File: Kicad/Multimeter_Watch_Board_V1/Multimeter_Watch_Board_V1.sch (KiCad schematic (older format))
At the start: 30 parts, among them J1 AudioJack3_Ground_renamedPins, J2 AudioJack3_Ground_renamedPins, J3 AudioJack3_Ground_renamedPins, J4 Conn_01x16_Female, J5 Conn_01x16_Female, U1 PCF85163-SO08, U2 AD8592, Y1 32kHz

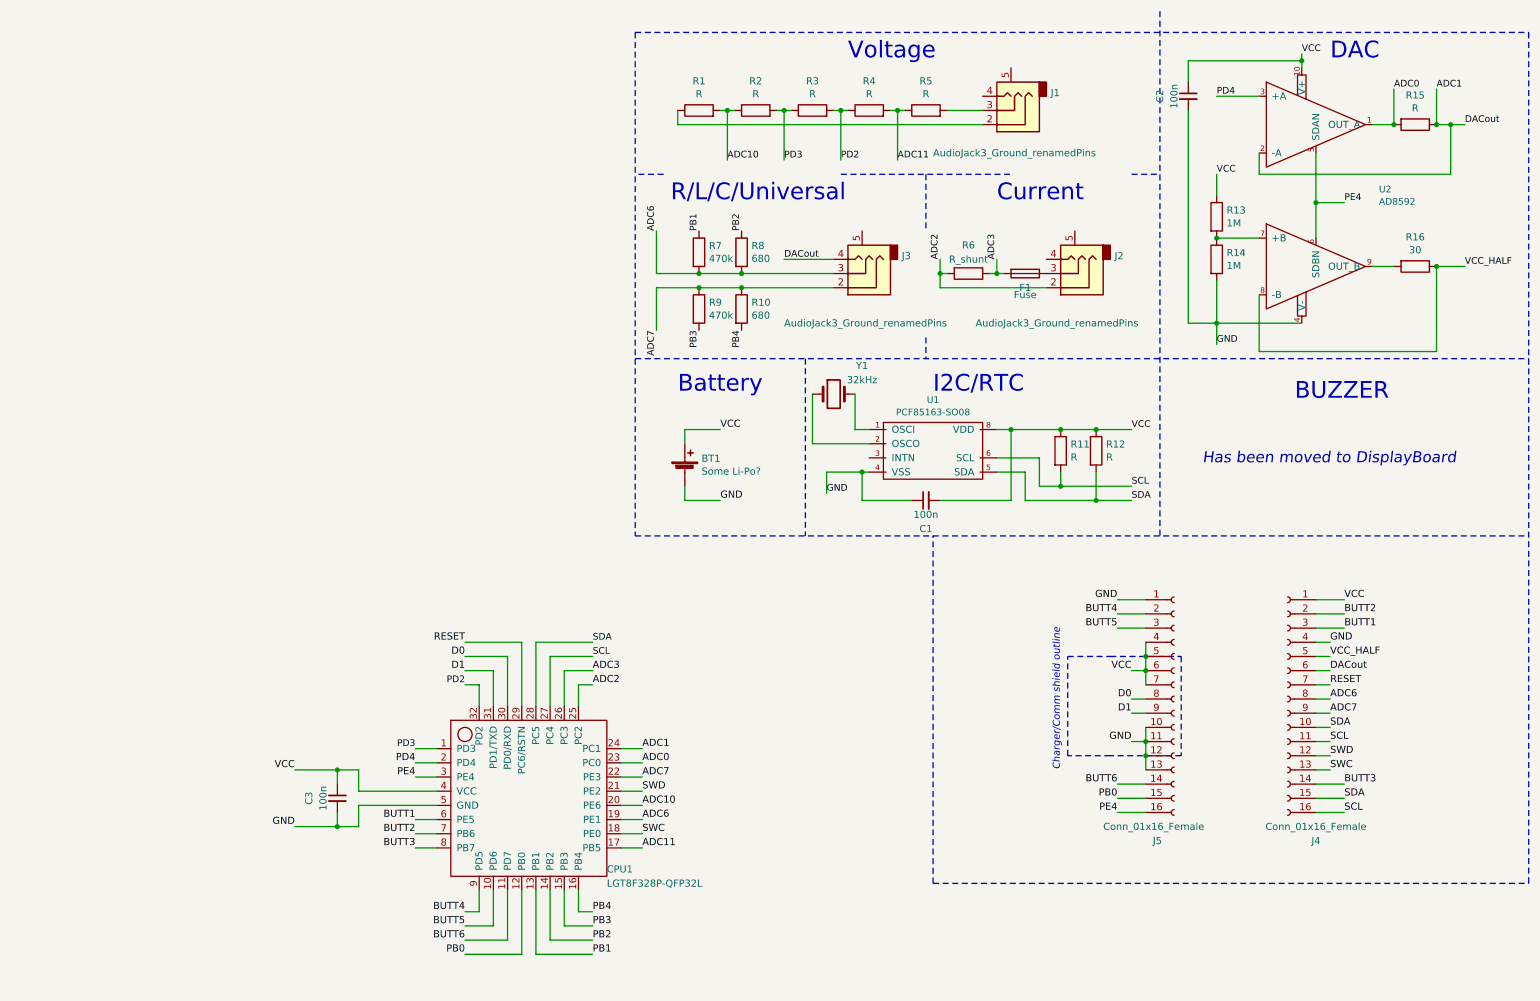
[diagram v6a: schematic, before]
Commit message: second layout attempt, various pinout changes for better routing
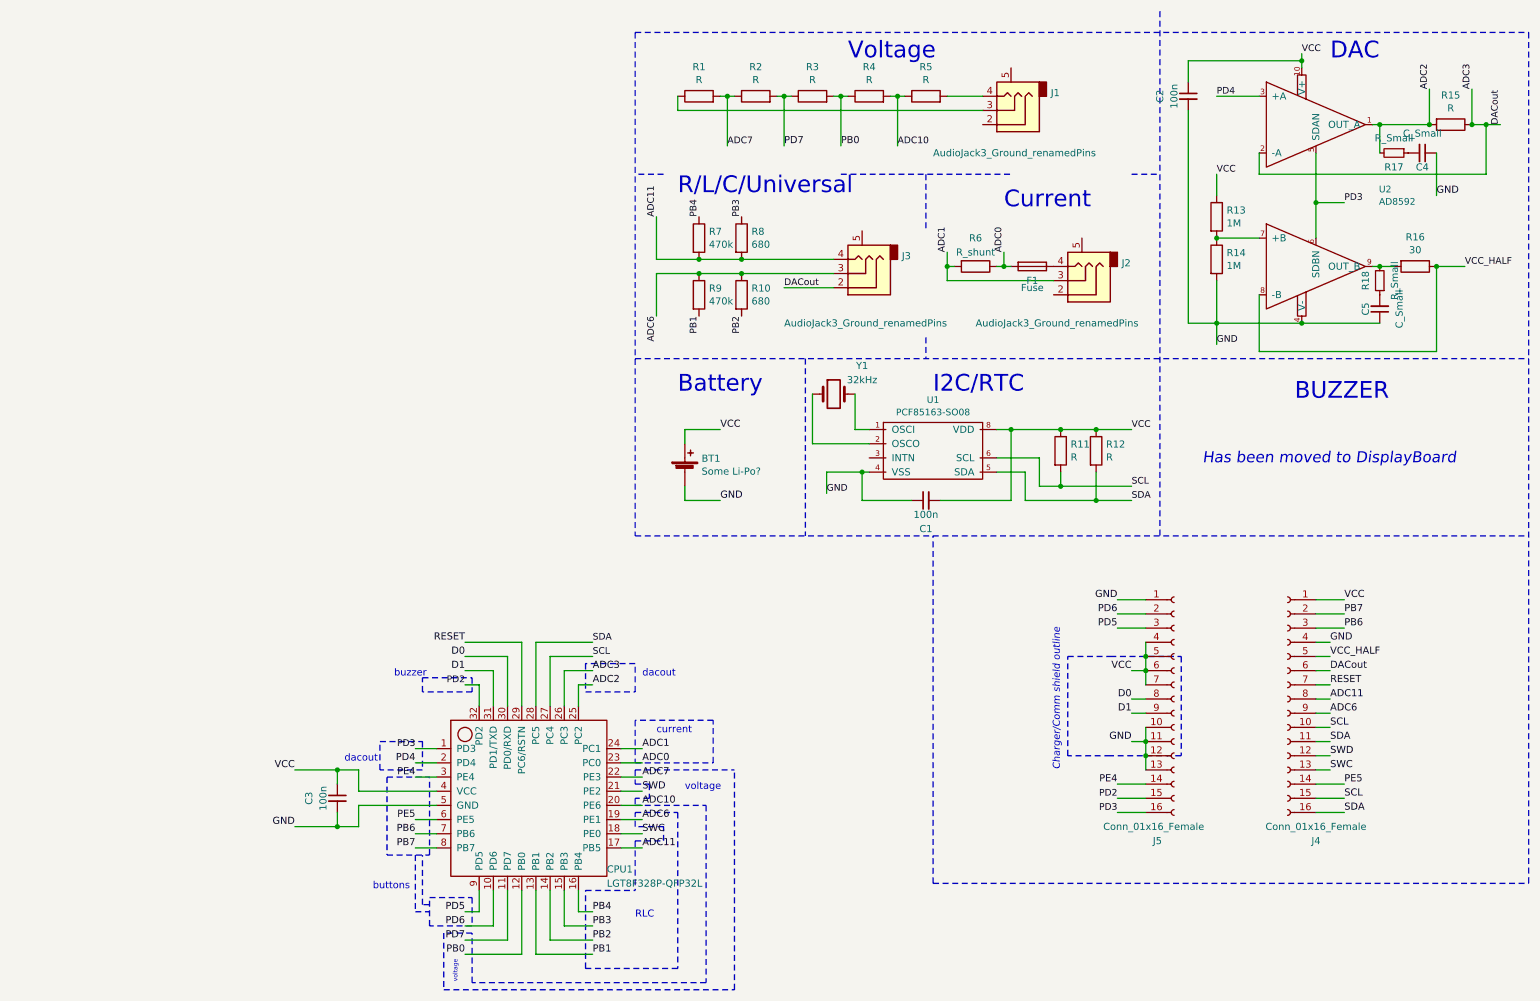
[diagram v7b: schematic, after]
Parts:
- added C4, C5: C_Small, Capacitor_SMD:C_0805_2012Metric_Pad1.15x1.40mm_HandSolder, symbol Device:C_Small
- added R17, R18: R_Small, Resistor_SMD:R_0805_2012Metric_Pad1.15x1.40mm_HandSolder, symbol Device:R_Small
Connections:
- net ADC0: now also F1.2, R6.1; no longer R15.2, U2.1 (OUT_A)
- net ADC1: now also J2.3, R6.2; no longer J3.4, J4.6 (Pin_6), R15.1, U2.2 (-A)
- net ADC10: now also R4.2, R5.1; no longer R1.2, R2.1
- net ADC11: now also J3.4, J4.8 (Pin_8), R7.2, R8.2; no longer R4.2, R5.1
- net ADC2: now also R15.2, U2.1 (OUT_A), R17.2; no longer J2.2, R6.2
- net ADC3: now also J3.2, J4.6 (Pin_6), R15.1, U2.2 (-A); no longer F1.2, R6.1
- net ADC6: now also J4.9 (Pin_9), R10.1, R9.1; no longer J4.8 (Pin_8), R7.2, R8.2
- net ADC7: now also R1.2, R2.1; no longer J3.2, J4.9 (Pin_9), R10.1, R9.1
- net GND: now also C4.1, C5.1
- net PB0: now also R3.2, R4.1; no longer J5.15 (Pin_15)
- net PB1: now also R9.2; no longer R7.1
- net PB2: now also R10.2; no longer R8.1
- net PB3: now also R8.1; no longer R9.2
- net PB4: now also R7.1; no longer R10.2
- net PD2: now also J5.15 (Pin_15); no longer R3.2, R4.1
- net PD3: now also J5.16 (Pin_16), U2.5 (SDAN), U2.6 (SDBN); no longer R2.2, R3.1
- net PE4: now also J5.14 (Pin_14); no longer J5.16 (Pin_16), U2.5 (SDAN), U2.6 (SDBN)
- net SCL: now also J4.10 (Pin_10), J4.15 (Pin_15); no longer J4.11 (Pin_11), J4.16 (Pin_16)
- net SDA: now also J4.11 (Pin_11), J4.16 (Pin_16); no longer J4.10 (Pin_10), J4.15 (Pin_15)
- net at R5.2: now also J1.4; no longer J1.3
- net at R1.1: now also J1.3; no longer J1.2
- net at F1.1: now also J2.4; no longer J2.3
- net at R16.2, U2.9 (OUT_B): now also R18.2
- net BUTT1 renamed PB6
- net PB6: now also CPU1.7 (PB6); no longer CPU1.6 (PE5)
- net BUTT2 renamed PB7
- net PB7: now also CPU1.8 (PB7); no longer CPU1.7 (PB6)
- net BUTT3 renamed PE5
- net PE5: now also CPU1.6 (PE5); no longer CPU1.8 (PB7)
- net BUTT4 renamed PD5
- net PD5: now also J5.3 (Pin_3); no longer J5.2 (Pin_2)
- net BUTT5 renamed PD6
- net PD6: now also J5.2 (Pin_2); no longer J5.3 (Pin_3)
- net BUTT6 renamed PD7
- net PD7: now also R2.2, R3.1; no longer J5.14 (Pin_14)
- new net: C4.2, R17.1
- new net: C5.2, R18.1
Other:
- note added: "RLC\n"
- note added: "buttons\n"
- note added: "buzzer"
- note added: "current\n"
- note added: "dacout"
- note added: "dacout\n"
- note added: "voltage\n"
- moved on the sheet: F1, J2, R1, R10, R15, R2, R3, R4, R5, R6, R7, R8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

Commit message: move I2C pullups from VCC to enable
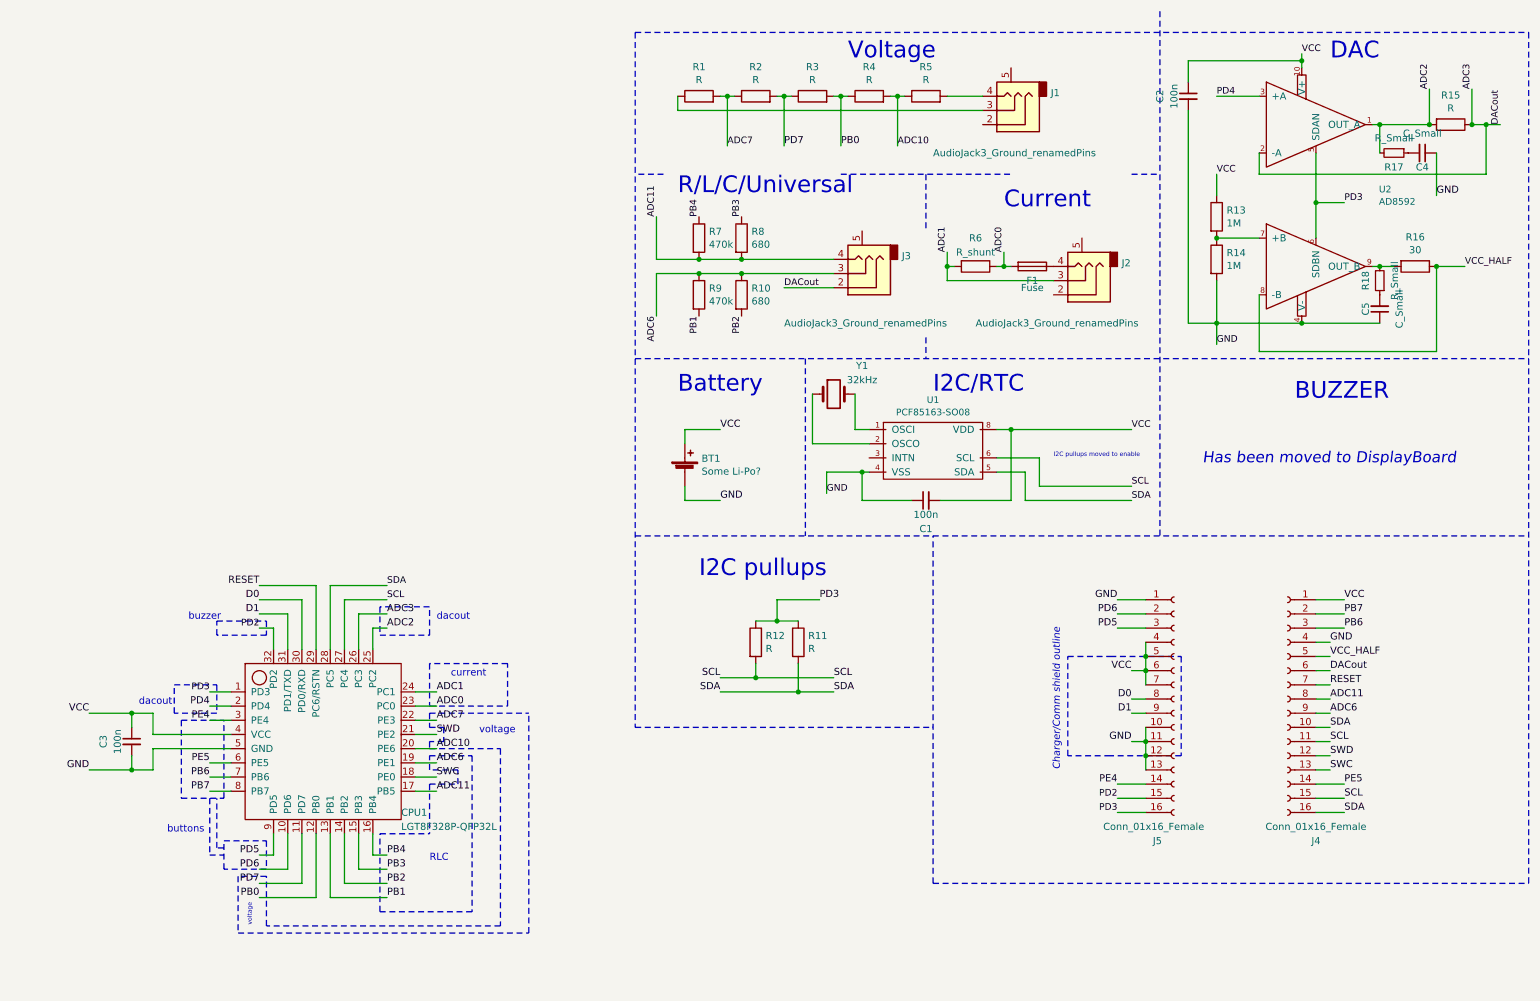
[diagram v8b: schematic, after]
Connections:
- net PD3: now also R11.1, R12.1
- net SCL: now also J4.11 (Pin_11), R12.2; no longer J4.10 (Pin_10), R11.2
- net SDA: now also J4.10 (Pin_10), R11.2; no longer J4.11 (Pin_11), R12.2
- net VCC: no longer R11.1, R12.1
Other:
- note added: "I2C pullups"
- note added: "I2C pullups moved to enable"
- moved on the sheet: C3, CPU1, R11, R12
